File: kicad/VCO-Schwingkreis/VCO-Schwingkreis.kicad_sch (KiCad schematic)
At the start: 8 parts, among them Q1 NMOS, Q2 NMOS

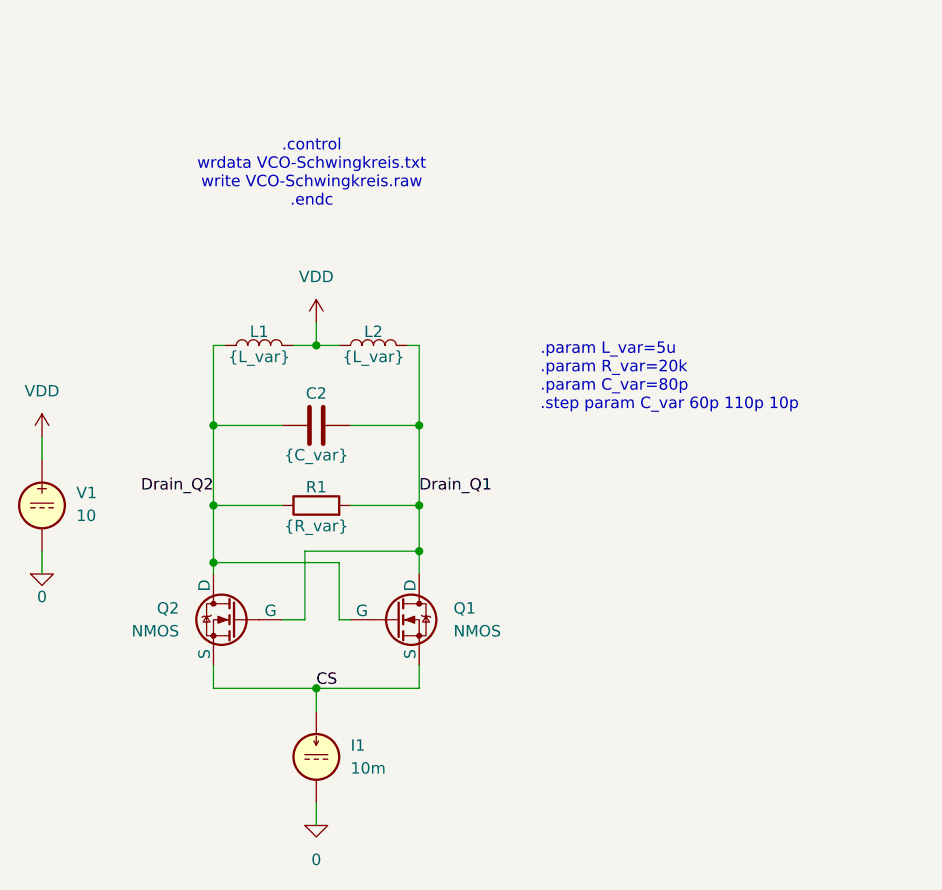
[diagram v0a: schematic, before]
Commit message: Kapazitätsdiode eingebaut
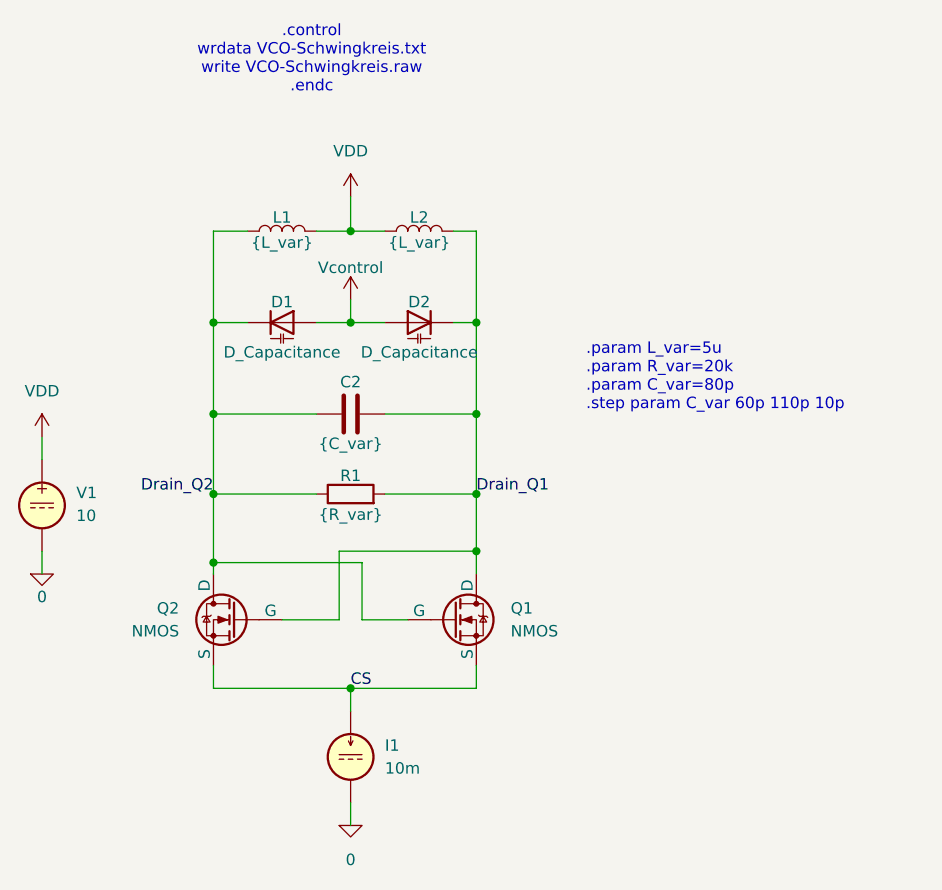
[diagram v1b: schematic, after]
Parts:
- added D1, D2: D_Capacitance, symbol Device:D_Capacitance
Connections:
- net Drain_Q1: now also D2.1 (K)
- net Drain_Q2: now also D1.1 (K)
- new net Vcontrol: D1.2 (A), D2.2 (A)
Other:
- moved on the sheet: C2, I1, L1, L2, Q1, R1

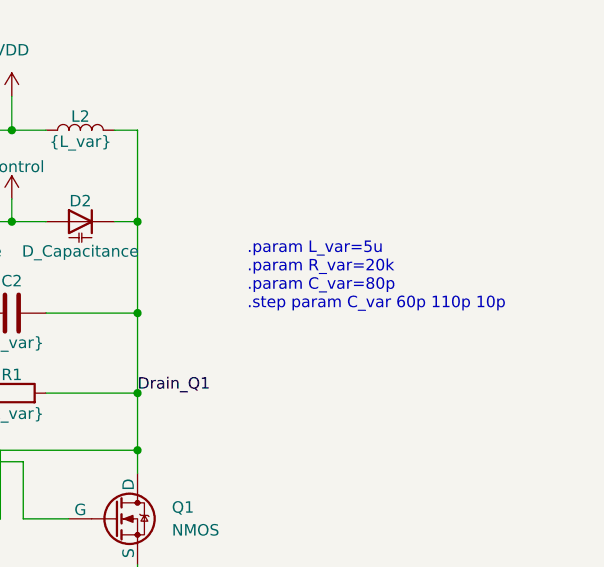
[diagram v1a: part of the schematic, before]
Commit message: Wien-Brücken-Oszillator hinzugefügt
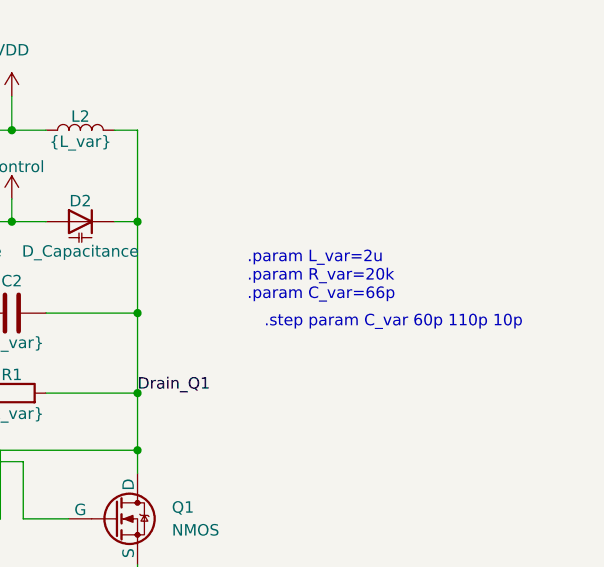
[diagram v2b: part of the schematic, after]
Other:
- note added: ".param L_var=2u .param R_var=20k .param C_var=66p"
- note added: ".step param C_var 60p 110p 10p"
- note removed: ".param L_var=5u .param R_var=20k .param C_var=80p .step param C_var 60p 110p 10p"
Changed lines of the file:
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@@
 	(generator_version "10.0")
 	(paper "A4")
-	(text ".param L_var=5u\n.param R_var=20k\n.param C_var=80p\n.step param C_var 60p 110p 10p"
+	(text ".param L_var=2u\n.param R_var=20k\n.param C_var=66p\n"
 		(exclude_from_sim no)
 		(at 176.022 61.976 0)
@@
 		(effects
 			(font
+				(size 1.27 1.27)
+			)
+		)
+	)
+	(text ".step param C_var 60p 110p 10p"
+		(exclude_from_sim yes)
+		(at 192.278 67.056 0)
+		(effects
+			(font
